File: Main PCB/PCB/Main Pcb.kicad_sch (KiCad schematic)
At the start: 9 parts, among them U1 2590, U2 DRV8825_STEPPER_MOTOR_DRIVER_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, U3 DRV8825_STEPPER_MOTOR_DRIVER_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

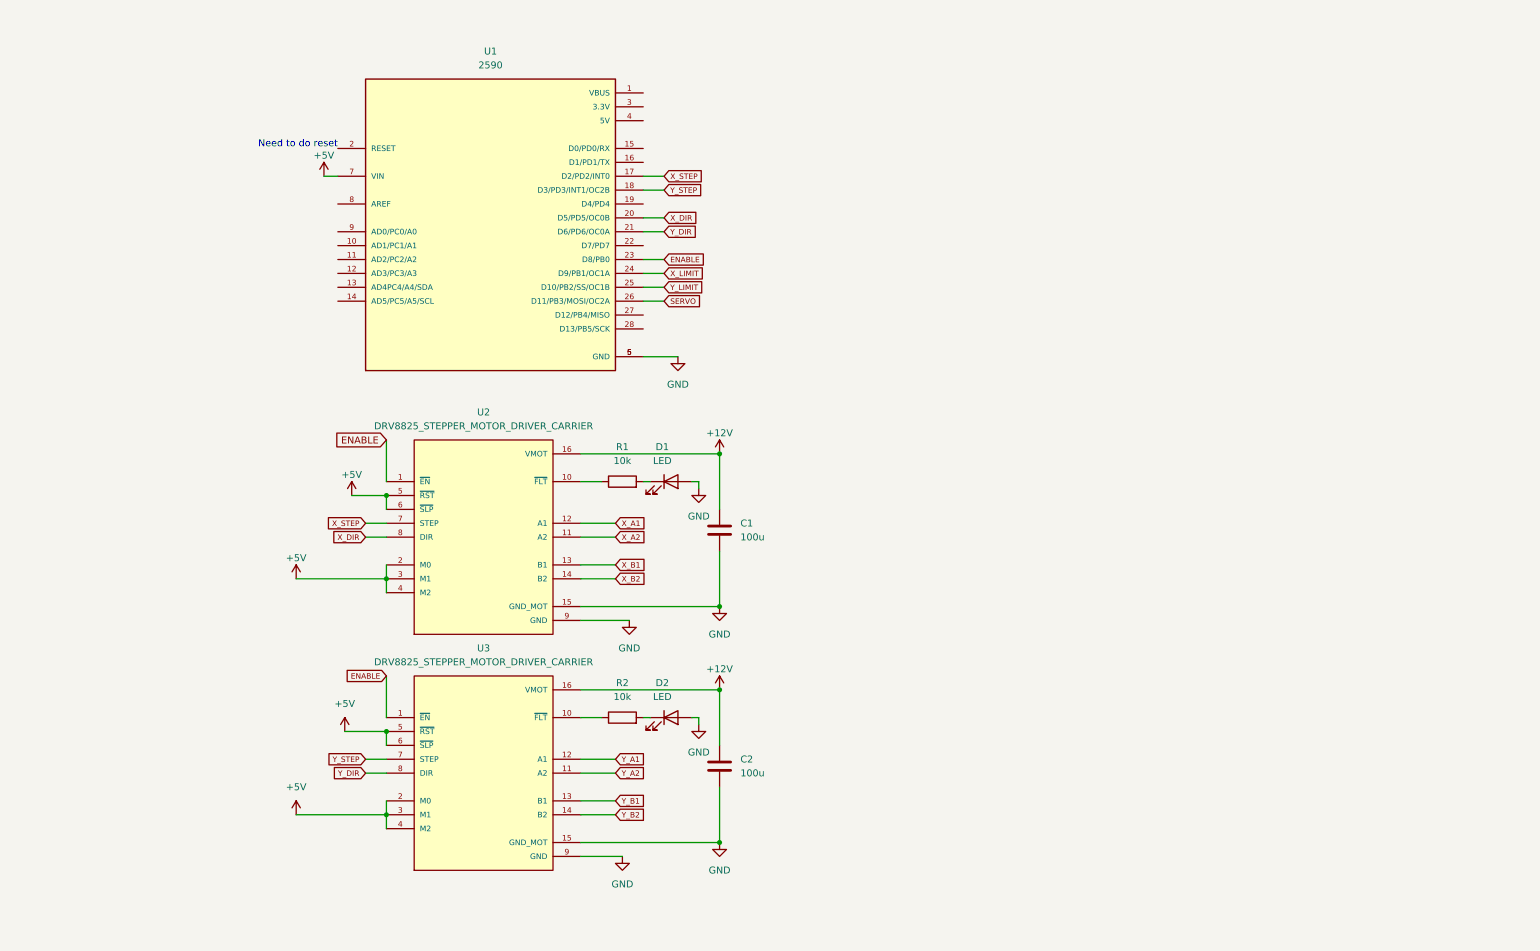
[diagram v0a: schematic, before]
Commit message: Add files via upload
added Paper Roller, Volt level Shifter I2C, 12v to 5v Converter, Reset Switch, and wired raspberry pi
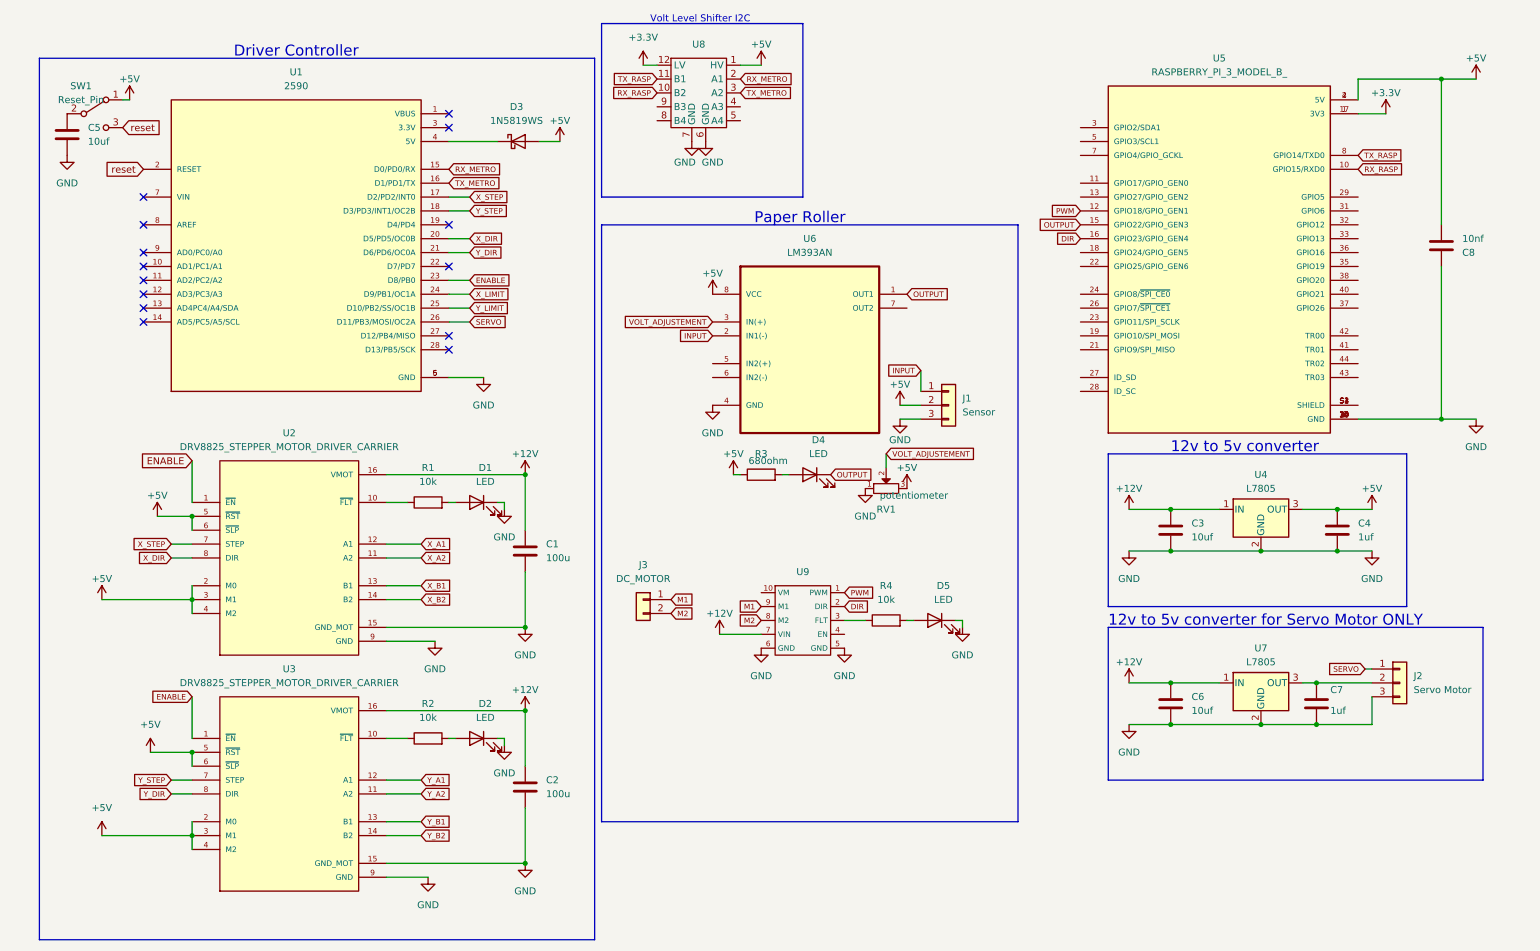
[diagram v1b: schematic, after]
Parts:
- added C3, C5, C6: 10uf, Main Library:100u, symbol Device:C
- added C4, C7: 1uf, Main Library:100u, symbol Device:C
- added C8: 10nf, Main Library:100u, symbol Device:C
- added D3: 1N5819WS, Diode_SMD:D_SOD-323, symbol Diode:1N5819WS
- added D4, D5: LED, symbol Device:LED
- added J1: Sensor, symbol Connector_Generic:Conn_01x03
- added J2: Servo Motor, symbol Connector_Generic:Conn_01x03
- added J3: DC_MOTOR, symbol Connector_Generic:Conn_01x02
- added R3: 680ohm, Main Library:100u, symbol Device:R
- added R4: 10k, Main Library:100u, symbol Device:R
- added RV1: potentiometer, PCM_SL_Footprints:potentiometer_3362P, symbol PCM_SL_Devices:potentiometer_3362P
- added SW1: Reset_Pin, symbol Switch:SW_SPDT
- added U4, U7: L7805, Main Library:L7805, symbol Regulator_Linear:L7805
- added U5: RASPBERRY_PI_3_MODEL_B_, RASPBERRY_PI_3_MODEL_B_:MODULE_RASPBERRY_PI_3_MODEL_B_, symbol Main_Library:RASPBERRY_PI_3_MODEL_B_
- added U6: LM393AN, Main Library:LM393AN, symbol Main_Library:LM393AN
- added U8: ~, Main Library:VOLTAGE LEVEL SHIFTER CONVERTER, symbol Main_Library:LEVEL_CONVERTER
- added U9: ~, Main Library:DC_MOTOR_DRIVER, symbol Main_Library:DC_MOTOR_DRIVER
- C1, C2, R1, R2: footprint (none) -> Main Library:100u
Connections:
- net +12V: now also C3.1, C6.1, U4.1 (IN), U7.1 (IN), U9.7 (VIN)
- net +5V: now also C4.1, C8.2, D3.2 (A), J1.2 (Pin_2), R3.1, RV1.3, SW1.1 (A), U4.3 (OUT), U5.2 (5V), U5.4 (5V), U6.8 (VCC), U8.1 (HV); no longer U1.7 (VIN)
- net GND: now also D1.1 (K), D2.1 (K), C3.2, C4.2, C5.2, C6.2, C7.2, C8.1, D5.1 (K), J1.3 (Pin_3), J2.3 (Pin_3), RV1.1, U4.2 (GND), U5.14 (GND), U5.20 (GND), U5.25 (GND), U5.30 (GND), U5.34 (GND), U5.39 (GND), U5.6 (GND), U5.9 (GND), U6.4 (GND), U7.2 (GND), U8.6 (GND), U8.7 (GND), U9.5 (GND), U9.6 (GND); no longer D1.2 (A), D2.2 (A)
- net SERVO: now also J2.1 (Pin_1)
- net at R2.2: now also D2.2 (A); no longer D2.1 (K)
- net RX_METRO: now reaches U1.15 (D0/PD0/RX)
- net RX_METRO: now also U8.2 (A1)
- net TX_METRO: now reaches U1.16 (D1/PD1/TX)
- net TX_METRO: now also U8.3 (A2)
- net reset: now reaches U1.2 (RESET)
- net reset: now also SW1.3 (C)
- net at U1.4 (5V): now also D3.1 (K)
- net at R1.2: now also D1.2 (A); no longer D1.1 (K)
- new net: D4.2 (A), R3.2
- new net: C7.1, J2.2 (Pin_2), U7.3 (OUT)
- new net: U5.S1 (SHIELD), U5.S2 (SHIELD), U5.S3 (SHIELD), U5.S4 (SHIELD)
- new net: C5.1, SW1.2 (B)
- new net: R4.1, U9.3 (FLT)
- new net: D5.2 (A), R4.2
- new net +3.3V: U5.1 (3V3), U5.17 (3V3), U8.12 (LV)
- new net DIR: U5.16 (GPIO23/GPIO_GEN4), U9.2 (DIR)
- new net INPUT: J1.1 (Pin_1), U6.2 (IN1(-))
- new net M1: J3.1 (Pin_1), U9.9 (M1)
- new net M2: J3.2 (Pin_2), U9.8 (M2)
- new net OUTPUT: D4.1 (K), U5.15 (GPIO22/GPIO_GEN3), U6.1 (OUT1)
- new net PWM: U5.12 (GPIO18/GPIO_GEN1), U9.1 (PWM)
- new net RX_RASP: U5.10 (GPIO15/RXD0), U8.10 (B2)
- new net TX_RASP: U5.8 (GPIO14/TXD0), U8.11 (B1)
- new net VOLT_ADJUSTEMENT: RV1.2, U6.3 (IN(+))
- no-connect marks 0 -> 14
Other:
- note added: "12v to 5v converter"
- note added: "12v to 5v converter for Servo Motor ONLY"
- note added: "Driver Controller"
- note added: "Paper Roller"
- note added: "Volt Level Shifter I2C"
- note removed: "Need to do reset"
- moved on the sheet: C1, C2, R1, R2, U1, U2, U3

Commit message: Add files via upload
added all parts needed for the PenPlotter. PCB Design and Routing done.
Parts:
- removed C5: 10uf, Main Library:100u, symbol Device:C
- removed SW1: Reset_Pin, symbol Switch:SW_SPDT
- added J4: Barrel_Jack_Switch_Pin3Ring, Connector_BarrelJack:BarrelJack_Kycon_KLDX-0202-xC_Horizontal, symbol Connector:Barrel_Jack_Switch_Pin3Ring
- added J5, J6: Conn_01x04, Connector_PinHeader_2.54mm:PinHeader_1x04_P2.54mm_Horizontal, symbol Connector_Generic:Conn_01x04
- added R5: 10k, Main Library:100u, symbol Device:R
- D1, D2, D4, D5: footprint (none) -> LED_THT:LED_D3.0mm
- D3: footprint Diode_SMD:D_SOD-323 -> Diode_THT:D_DO-15_P10.16mm_Horizontal
- J1: footprint (none) -> Connector_PinSocket_2.54mm:PinSocket_1x03_P2.54mm_Horizontal
- J2: footprint (none) -> Connector_PinSocket_2.54mm:PinSocket_1x03_P2.54mm_Vertical
- J3: footprint (none) -> Connector_PinSocket_2.54mm:PinSocket_2x01_P2.54mm_Vertical
- U1: footprint footprint:MODULE_2590 -> Main Library:Metro Mini
- U2, U3: footprint footprint:IC_DRV8825_STEPPER_MOTOR_DRIVER_CARRIER -> Main Library:DRV8825
- U5: footprint RASPBERRY_PI_3_MODEL_B_:MODULE_RASPBERRY_PI_3_MODEL_B_ -> Main Library:RASPBERRY_PI_3_MODEL_B_
- U8: value ~ -> Voltage Converter
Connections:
- net +12V: now also J4.1
- net +5V: now also RV1.2; no longer RV1.3
- net GND: now also RV1.3, J4.2, J4.3, R5.1; no longer RV1.1
- net VOLT_ADJUSTEMENT: now also RV1.1; no longer RV1.2
- net reset: now also U8.4 (B3), R5.2
- net GPIO24: now reaches U5.18 (GPIO24/GPIO_GEN5)
- net GPIO24: now also U8.9 (A3)
- net X_A1: no longer names the net of U2.12 (A1)
- net X_A1: now also J6.1 (Pin_1)
- net X_A2: no longer names the net of U2.11 (A2)
- net X_A2: now also J6.2 (Pin_2)
- net X_B1: no longer names the net of U2.13 (B1)
- net X_B1: now also J6.3 (Pin_3)
- net X_B2: no longer names the net of U2.14 (B2)
- net X_B2: now also J6.4 (Pin_4)
- net Y_A1: no longer names the net of U3.12 (A1)
- net Y_A1: now also J5.1 (Pin_1)
- net Y_A2: no longer names the net of U3.11 (A2)
- net Y_A2: now also J5.2 (Pin_2)
- net Y_B1: no longer names the net of U3.13 (B1)
- net Y_B1: now also J5.3 (Pin_3)
- net Y_B2: no longer names the net of U3.14 (B2)
- net Y_B2: now also J5.4 (Pin_4)
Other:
- moved on the sheet: RV1, U8
